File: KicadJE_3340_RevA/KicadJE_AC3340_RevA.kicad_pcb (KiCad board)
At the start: 2 copper layers, 200 x 128 mm, 127 parts, among them J101 RampOut1, J102 PulseOut2, J103 SawOut3, J104 In1.1, J105 In1.2, J106 In1.3, J107 SS_In2, J108 HS_In3, J109 FM_In4, J110 PWM_In5, J111 SineOut4, P101 HEADER_2x5_Doepfer, Q101 MMBT3906, Q102 UMX1N, SW101 Octave (3 state), U101 TL072, U102 TL072, U103 TL072, U104 AS3340, U105 L78L05_SOT89, U106 L79L05_SOT89, U107 TL072

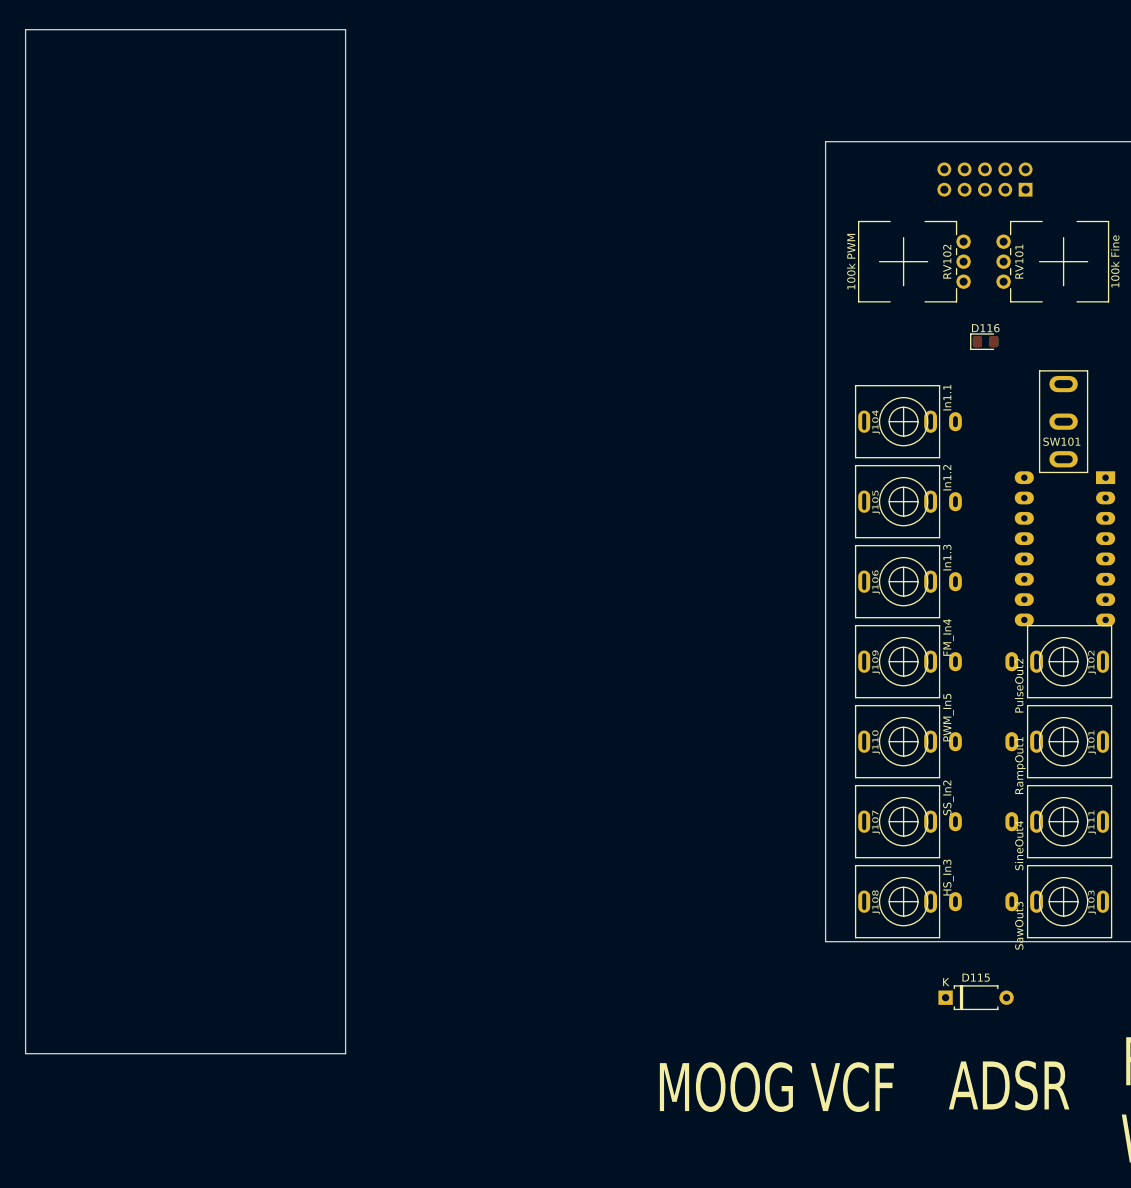
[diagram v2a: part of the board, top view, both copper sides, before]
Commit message: Update KicadJE_AC3340_RevA.kicad_pcb
Faceplate labels
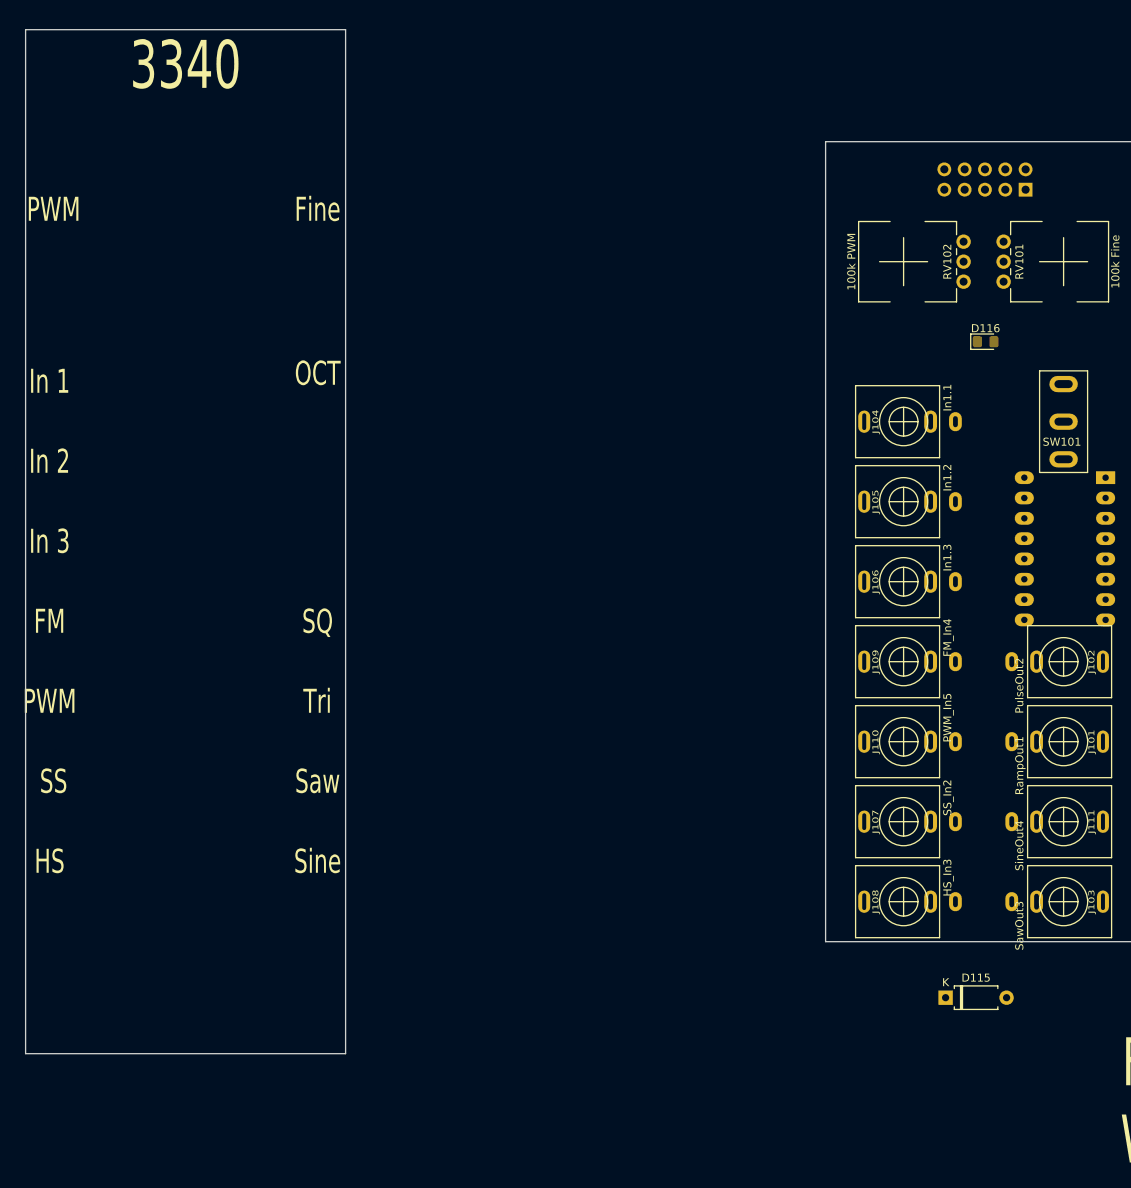
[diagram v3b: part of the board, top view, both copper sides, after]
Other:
- board text added: "3340"
- board text added: "FM"
- board text added: "Fine"
- board text added: "HS"
- board text added: "In 1"
- board text added: "In 2"
- board text added: "In 3"
- board text added: "OCT"
- board text added: "PWM"
- board text added: "SQ"
- board text added: "SS"
- board text added: "Saw"
- board text added: "Sine"
- board text added: "Tri"
- board text removed: "MOOG VCF"
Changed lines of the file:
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@@
   (general
     (thickness 1.6)
-    (drawings 83)
+    (drawings 96)
     (tracks 0)
     (zones 0)
@@
     )
   )
+  (gr_text PWM (at -47 120) (layer F.SilkS)
+    (effects (font (size 3 2) (thickness 0.5)))
+  )
+  (gr_text SS (at -46.5 130) (layer F.SilkS)
+    (effects (font (size 3 2) (thickness 0.5)))
+  )
+  (gr_text HS (at -47 140) (layer F.SilkS)
+    (effects (font (size 3 2) (thickness 0.5)))
+  )
+  (gr_text "In 1" (at -47 80) (layer F.SilkS)
+    (effects (font (size 3 2) (thickness 0.5)))
+  )
+  (gr_text "In 2" (at -47 90) (layer F.SilkS)
+    (effects (font (size 3 2) (thickness 0.5)))
+  )
+  (gr_text "In 3" (at -47 100) (layer F.SilkS)
+    (effects (font (size 3 2) (thickness 0.5)))
+  )
+  (gr_text FM (at -47 110) (layer F.SilkS)
+    (effects (font (size 3 2) (thickness 0.5)))
+  )
+  (gr_text Sine (at -13.5 140) (layer F.SilkS)
+    (effects (font (size 3 2) (thickness 0.5)))
+  )
+  (gr_text Saw (at -13.5 130) (layer F.SilkS)
+    (effects (font (size 3 2) (thickness 0.5)))
+  )
+  (gr_text Tri (at -13.5 120) (layer F.SilkS)
+    (effects (font (size 3 2) (thickness 0.5)))
+  )
+  (gr_text SQ (at -13.5 110) (layer F.SilkS)
+    (effects (font (size 3 2) (thickness 0.5)))
+  )
+  (gr_text OCT (at -13.5 79) (layer F.SilkS)
+    (effects (font (size 3 2) (thickness 0.5)))
+  )
+  (gr_text Fine (at -13.5 58.5) (layer F.SilkS)
+    (effects (font (size 3 2) (thickness 0.5)))
+  )
   (gr_line (start -16.5 36) (end -16.5 164) (layer Dwgs.User) (width 0.15))
   (gr_line (start -43.5 36) (end -43.5 164) (layer Dwgs.User) (width 0.15))
@@
     (effects (font (size 6 4) (thickness 1)) (justify mirror))
   )
-  (gr_text ADSR (at 73 168.2) (layer F.SilkS)
+  (gr_text 3340 (at -30 40.5) (layer F.SilkS)
     (effects (font (size 6 4) (thickness 1)))
   )
@@
     (effects (font (size 1.3 1.2) (thickness 0.3)) (justify left mirror))
   )
-  (gr_text "MOOG VCF" (at 43.8 168.4) (layer F.SilkS)
-    (effects (font (size 6 4) (thickness 1)))
+  (gr_text PWM (at -46.5 58.5) (layer F.SilkS)
+    (effects (font (size 3 2) (thickness 0.5)))
   )
   (gr_line (start 50 70) (end 150 70) (layer Dwgs.User) (width 0.15))

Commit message: Update KicadJE_AC3340_RevA.kicad_pcb
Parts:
- added G***: LOGO, AJ:Johansen_engineering_logo_20mm, F.Cu at (-30.0, 160.5)
- added REF**: MountingHole_Eurorack2, AJ:MountingHole_Eurorack2, F.Cu at (-16.5, 38.5)
- added REF**: 6,3mm inner, AJ:Jack_6m3, F.Cu at (-40.0, 125.0)
- added REF**: 6,3mm inner, AJ:Jack_6m3, F.Cu at (-40.0, 105.0)
- added REF**: 6,3mm inner, AJ:Jack_6m3, F.Cu at (-40.0, 115.0)
- added REF**: 6,3mm inner, AJ:Jack_6m3, F.Cu at (-20.0, 115.0)
- added REF**: 6,3mm inner, AJ:Jack_6m3, F.Cu at (-20.0, 125.0)
- added REF**: 6,3mm inner, AJ:Jack_6m3, F.Cu at (-20.0, 135.0)
- added REF**: 6,3mm inner, AJ:Jack_6m3, F.Cu at (-40.0, 135.0)
- added REF**: 6,3mm inner, AJ:Jack_6m3, F.Cu at (-40.0, 145.0)
- added REF**: 6,3mm inner, AJ:Jack_6m3, F.Cu at (-20.0, 145.0)
- added REF**: MountingHole_Eurorack2, AJ:MountingHole_Eurorack2, F.Cu at (-43.5, 38.5)
- added REF**: MountingHole_Eurorack2, AJ:MountingHole_Eurorack2, F.Cu at (-16.5, 160.5)
- added REF**: MountingHole_Eurorack, AJ:MountingHole_Eurorack, F.Cu at (-43.5, 160.5)
- added REF**: 6,3mm inner pot, AJ:Pot_6m3_scale1, F.Cu at (-20.0, 65.0)
- added REF**: 6,3mm inner pot, AJ:Pot_6m3_scale1, F.Cu at (-40.0, 65.0)
- added REF**: 6,3mm inner pot, AJ:Pot_6m3, F.Cu at (-20.0, 85.0)
- added REF**: 6,3mm inner, AJ:Jack_6m3, F.Cu at (-40.0, 85.0)
- added REF**: 6,3mm inner, AJ:Jack_6m3, F.Cu at (-40.0, 95.0)
- moved J103 10.0 mm to (79.8, 135.0)
- moved J111 10.0 mm to (79.8, 145.0)
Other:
- board text added: "in"
- board text added: "out"

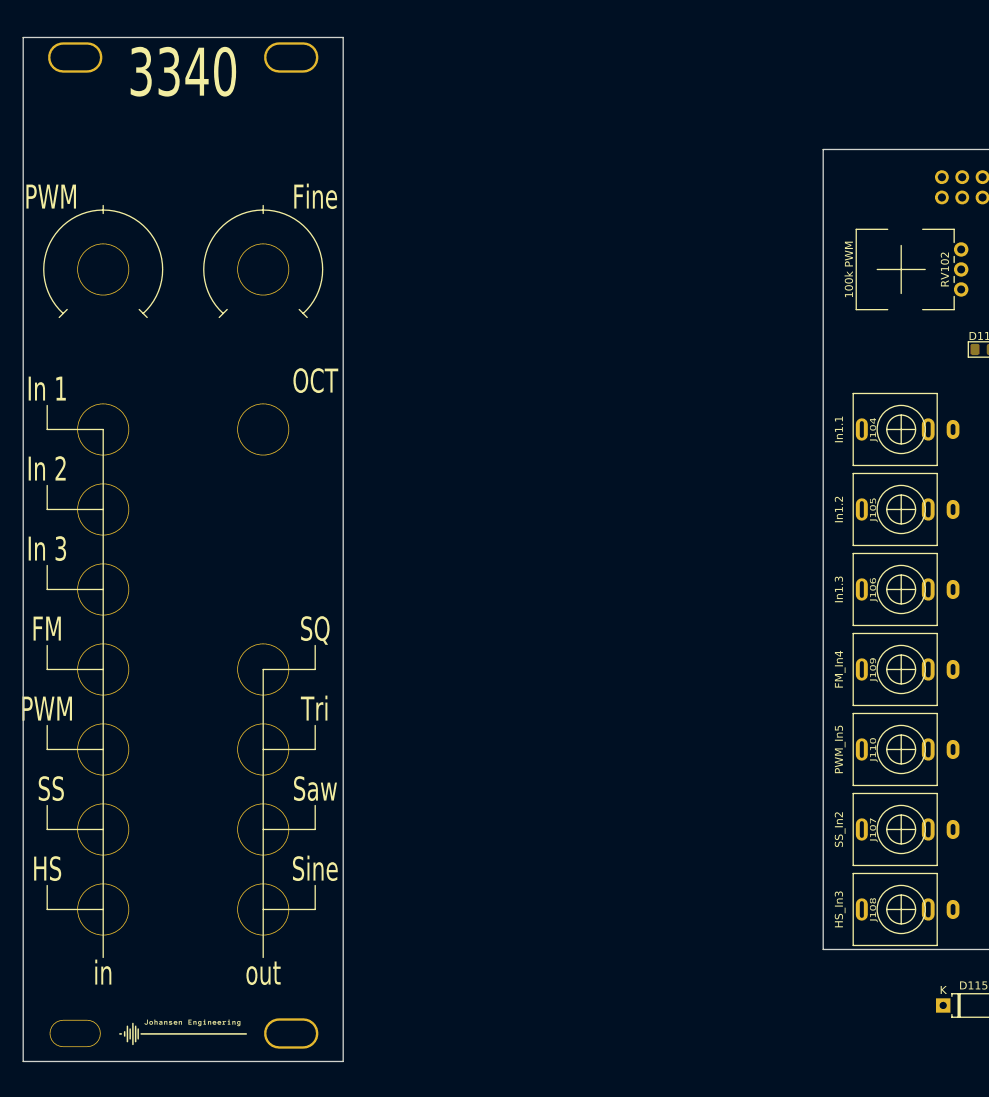
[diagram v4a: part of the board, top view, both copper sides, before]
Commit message: TP -> mounting holes + ERC
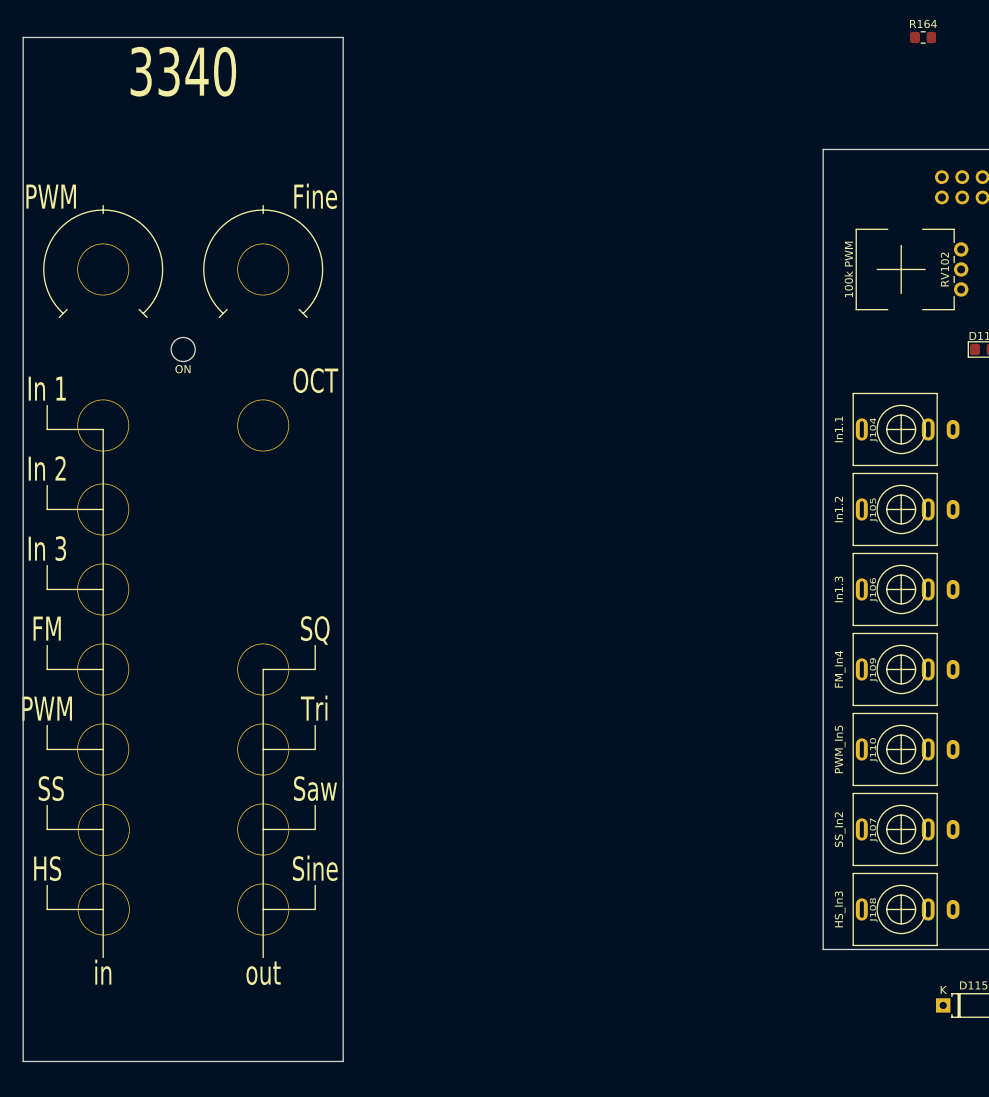
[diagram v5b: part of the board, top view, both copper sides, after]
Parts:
- removed G***: LOGO, AJ:Johansen_engineering_logo_20mm
- removed REF** (x3): MountingHole_Eurorack2, AJ:MountingHole_Eurorack2
- removed REF** (x11): 6,3mm inner, AJ:Jack_6m3
- removed REF**: MountingHole_Eurorack, AJ:MountingHole_Eurorack
- removed REF** (x2): 6,3mm inner pot, AJ:Pot_6m3_scale1
- removed REF**: 6,3mm inner pot, AJ:Pot_6m3
- added R164: 1k, Resistor_SMD:R_0805_2012Metric_Pad1.15x1.40mm_HandSolder, F.Cu at (62.5, 36.0)
- added TP101: Oct, AJ:Pot_6m3, F.Cu at (-20.0, 84.5)
- added TP102: In1, AJ:Jack_6m3, F.Cu at (-20.0, 125.0)
- added TP103: In2, AJ:Jack_6m3, F.Cu at (-39.9, 135.1)
- added TP104: In3, AJ:Jack_6m3, F.Cu at (-20.0, 145.0)
- added TP105: SS, AJ:Jack_6m3, F.Cu at (-20.0, 135.0)
- added TP106: HS, AJ:Jack_6m3, F.Cu at (-39.9, 145.0)
- added TP107: FM, AJ:Jack_6m3, F.Cu at (-20.0, 115.0)
- added TP108: PWM, AJ:Jack_6m3, F.Cu at (-40.0, 125.0)
- added TP109: Tri, AJ:Jack_6m3, F.Cu at (-40.0, 84.5)
- added TP110: SQ, AJ:Jack_6m3, F.Cu at (-40.0, 115.0)
- added TP111: Saw, AJ:Jack_6m3, F.Cu at (-40.0, 95.0)
- added TP112: Fine, AJ:Pot_6m3_scale1, F.Cu at (-40.0, 65.0)
- added TP113: PWM, AJ:Pot_6m3_scale1, F.Cu at (-20.0, 65.0)
- added TP114: ON, AJ:LED_Hole_3mm, F.Cu at (-30.0, 75.0)
- added TP115: 3m5 jack, AJ:Jack_6m3, F.Cu at (-40.0, 105.0)
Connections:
- D103 pad 2: 3CVIn1 -> Net-(D103-Pad2)
- D104 pad 1: 3CVIn1 -> Net-(D103-Pad2)
- R108 pad 1: 3CVIn1 -> Net-(D103-Pad2)
- R109 pad 1: 3CVIn1 -> Net-(D103-Pad2)
- R110 pad 1: 3CVIn1 -> Net-(D103-Pad2)
- R117 pad 1: 3CVIn1 -> Net-(D103-Pad2)
- R118 pad 2: 3CVIn1 -> Net-(D103-Pad2)

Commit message: Faceplate A2
change order of inputs
move octave
move led hole
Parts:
- removed TP114: ON, AJ:LED_Hole_3mm
- added H101: MountingHole_Pad, AJ:MountingHole_Eurorack3, F.Cu at (-43.5, 39.0)
- added H102: MountingHole_Pad, AJ:MountingHole_Eurorack3, B.Cu at (-43.5, 161.0)
- added H103: MountingHole_Pad, AJ:MountingHole_Eurorack3, F.Cu at (-16.5, 39.0)
- added H104: MountingHole_Pad, AJ:MountingHole_Eurorack3, B.Cu at (-16.5, 161.0)
- added H105: ON, AJ:LED_Hole_3mm, F.Cu at (-30.0, 75.0)
- R164: moved to B.Cu
- U104: moved to F.Cu
- moved U107 172.7 mm to (59.5, 76.0), turned to 180 degrees
- moved U102 129.8 mm to (62.0, 120.0), turned to 180 degrees
- moved U101 121.5 mm to (77.5, 120.0), turned to 180 degrees
- moved U103 28.1 mm to (176.5, 44.0)
- moved SW101 15.0 mm to (79.8, 100.0)
- moved U104 1.00 mm to (85.0, 91.0)
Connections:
- TP112 pad 1: (no net) -> GND
- TP113 pad 1: (no net) -> GND

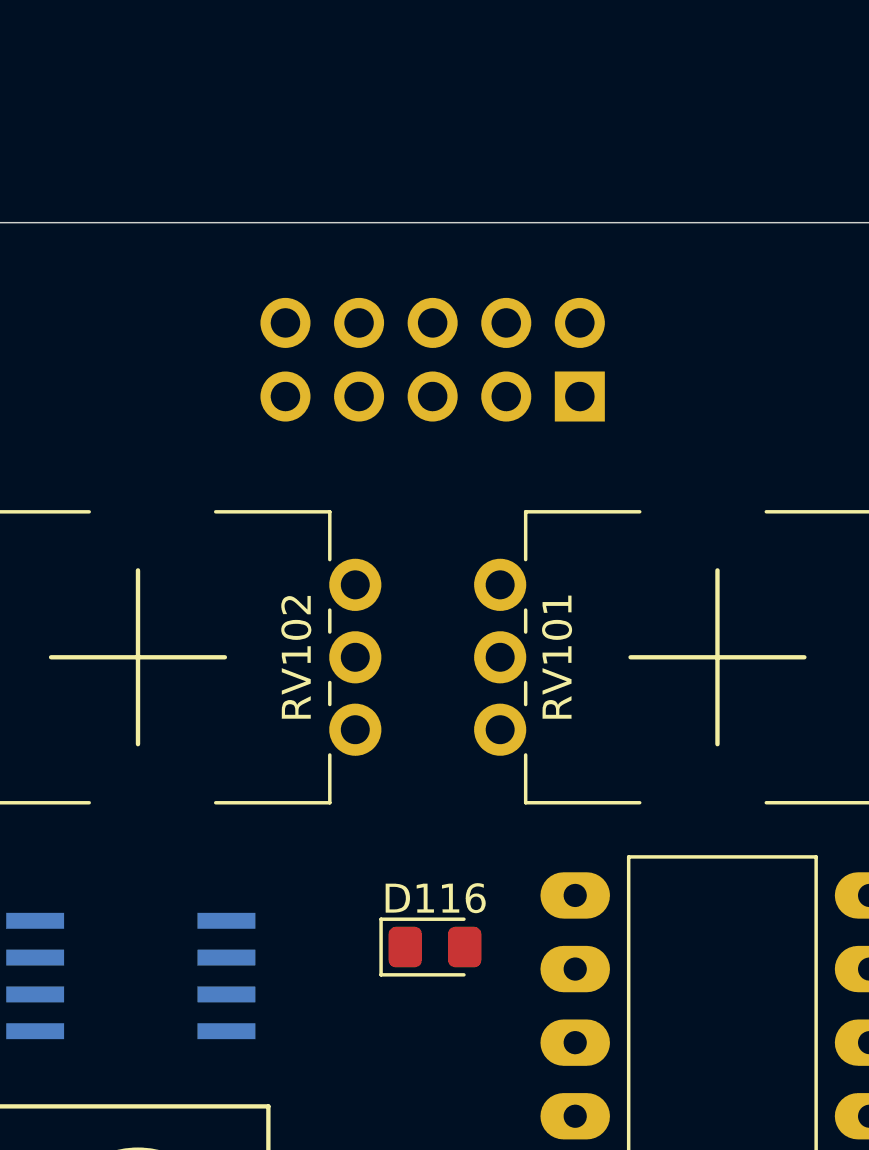
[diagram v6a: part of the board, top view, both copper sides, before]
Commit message: LED PWR moved
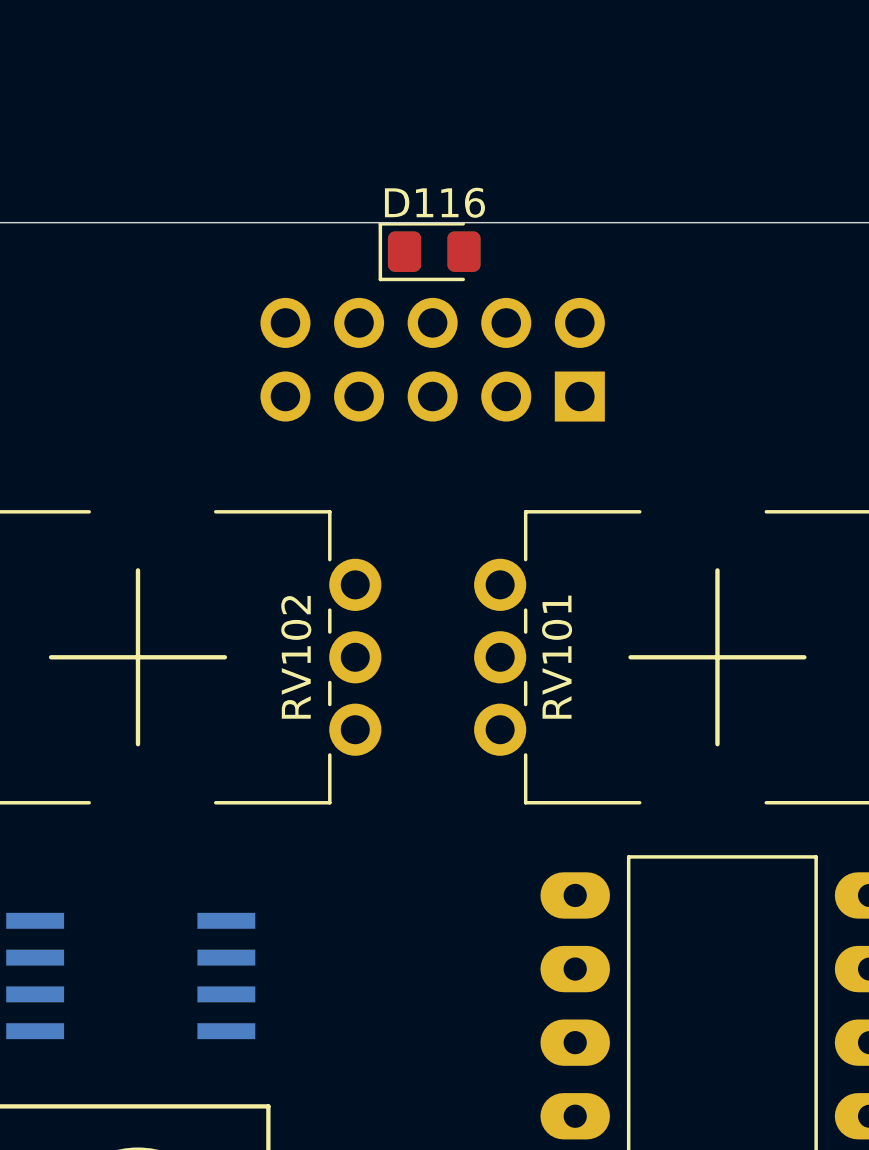
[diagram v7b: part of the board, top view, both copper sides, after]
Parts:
- moved D116 24.0 mm to (70.0, 51.0)
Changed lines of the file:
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@@
   )
   (module LED_SMD:LED_0805_2012Metric_Pad1.15x1.40mm_HandSolder (layer F.Cu)
-    (at 70 75)
+    (at 69.975 51)
     (descr "LED SMD 0805 (2012 Metric), square (rectangular) end terminal, IPC_7351 nominal, (Body size source: https://docs.google.com/spreadsheets/d/1BsfQQcO9C6DZCsRaXUlFlo91Tg2WpOkGARC1WS5S8t0/edit?usp=sharing), generated with kicad-footprint-generator")
     (tags "LED handsolder")

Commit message: main components placed
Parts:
- C112, C113, R138: moved to F.Cu
- moved RV103 188.8 mm to (45.9, 42.7)
- moved RV104 188.8 mm to (45.9, 36.3)
- moved C114 175.2 mm to (59.2, 8.00)
- moved JP101 175.1 mm to (71.2, 73.2)
- moved D108 175.0 mm to (82.2, 46.8)
- moved D117 175.0 mm to (76.5, 46.8)
- moved D118 175.0 mm to (76.5, 43.4)
- moved Q101 172.0 mm to (78.8, 74.2)
- moved D109 168.3 mm to (88.5, 31.5)
- moved D107 163.9 mm to (82.5, 38.7)
- moved C116 161.3 mm to (58.0, 16.0)
- moved C110 160.0 mm to (67.0, 78.2)
- moved C113 159.3 mm to (73.5, 58.5)
- moved C118 158.7 mm to (59.2, 4.00)
- moved R138 156.7 mm to (66.0, 51.0), turned to 180 degrees
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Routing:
- net -12VA: track 0.00 -> 137.0 mm, vias 0 -> 1
- net +12VA: track 0.00 -> 98.1 mm, vias 0 -> 2
- net GND: track 0.00 -> 26.6 mm
- net Net-(D116-Pad2): track 0.00 -> 1.70 mm
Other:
- outline, holes or cut-outs redrawn
